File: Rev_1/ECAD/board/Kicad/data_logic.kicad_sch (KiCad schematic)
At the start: 7 parts

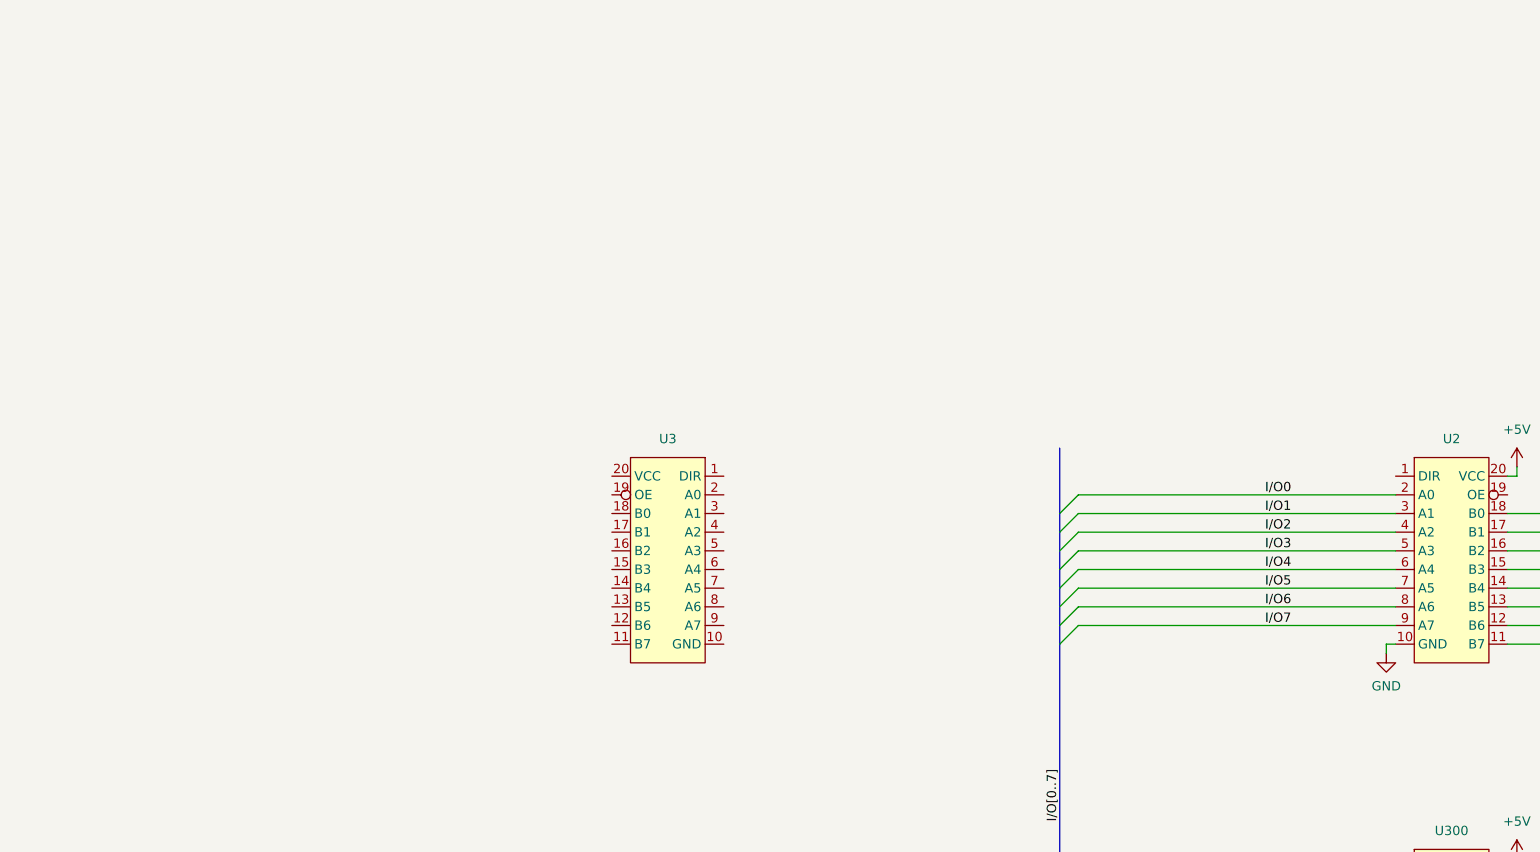
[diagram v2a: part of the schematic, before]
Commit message: Added Rotary encoder and buttons to the Input Buffer
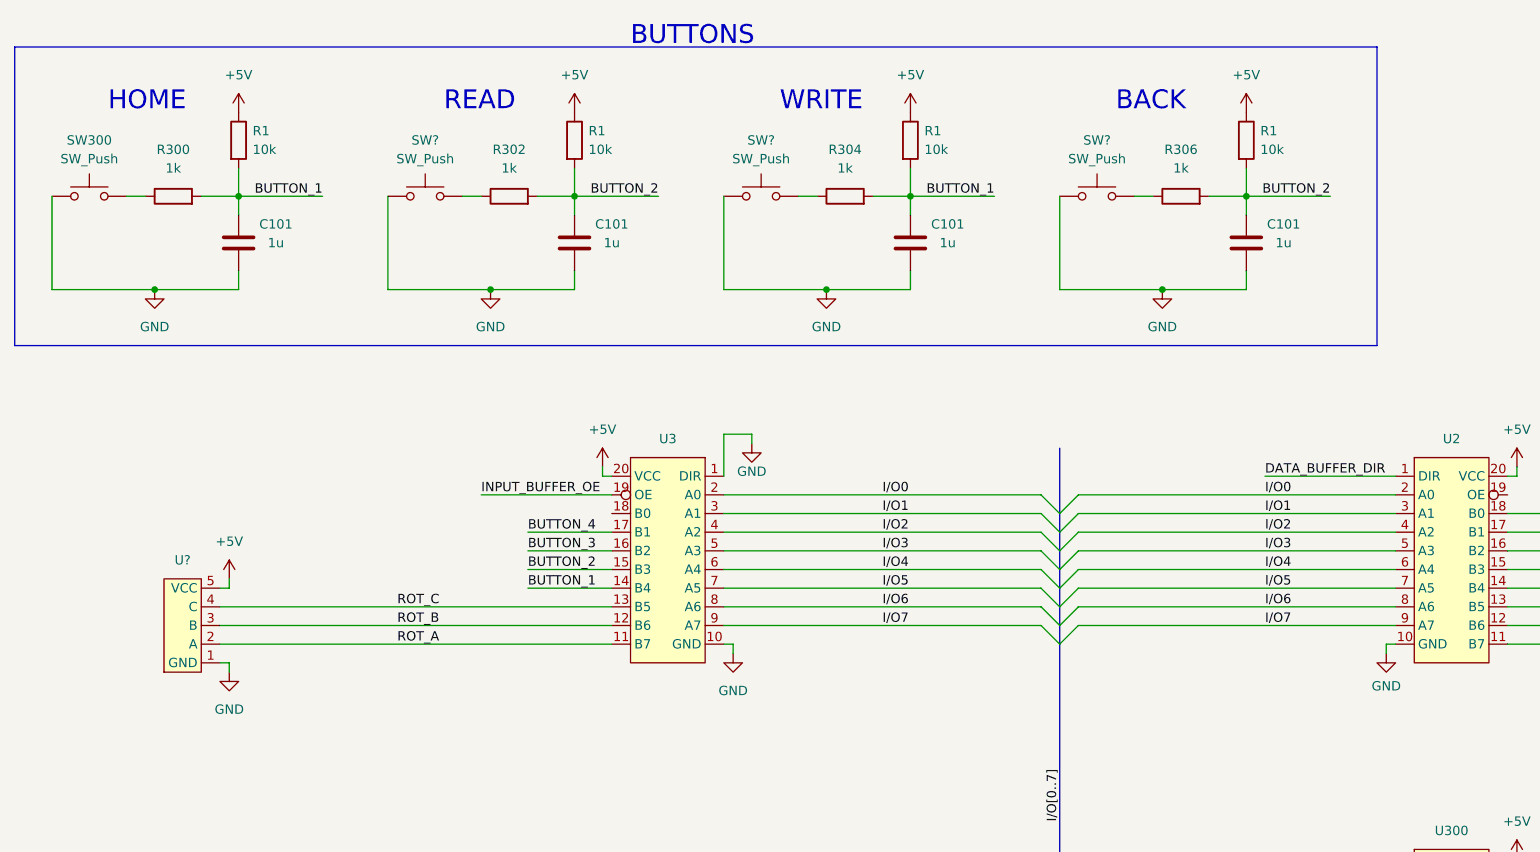
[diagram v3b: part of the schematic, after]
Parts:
- added C101 (x4): 1u, Capacitor_SMD:C_0805_2012Metric_Pad1.18x1.45mm_HandSolder, symbol Device:C
- added R1 (x4): 10k, Resistor_SMD:R_0805_2012Metric_Pad1.20x1.40mm_HandSolder, symbol Device:R
- added R300, R302, R304, R306: 1k, Resistor_SMD:R_0805_2012Metric_Pad1.20x1.40mm_HandSolder, symbol Device:R
- added SW300, SW? (x3): SW_Push, symbol Switch:SW_Push
- added U?: ~, symbol EEPROM_PROGRAMER:Rotary_Encoder
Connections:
- net +5V: now also U3.20 (VCC), R1.1, R1.1, R1.1, R1.1, U?.5 (VCC)
- net GND: now also U3.1 (DIR), U3.10 (GND), C101.1, C101.1, C101.1, C101.1, SW300.1, SW?.1, SW?.1, SW?.1, U?.1 (GND)
- net I/O0: now also U3.2 (A0)
- net I/O1: now also U3.3 (A1)
- net I/O2: now also U3.4 (A2)
- net I/O3: now also U3.5 (A3)
- net I/O4: now also U3.6 (A4)
- net I/O5: now also U3.7 (A5)
- net I/O6: now also U3.8 (A6)
- net I/O7: now also U3.9 (A7)
- net ROT_A: now reaches U3.11 (B7)
- net ROT_A: now also U?.2 (A)
- net ROT_B: now reaches U3.12 (B6)
- net ROT_B: now also U?.3 (B)
- net ROT_C: now reaches U3.13 (B5)
- net ROT_C: now also U?.4 (C)
- net BUTTON_1: now reaches U3.14 (B4)
- net BUTTON_1: now also C101.2, C101.2, R1.2, R1.2, R300.2, R304.2
- net BUTTON_2: now reaches U3.15 (B3)
- net BUTTON_2: now also C101.2, C101.2, R1.2, R1.2, R302.2, R306.2
- net BUTTON_3: now reaches U3.16 (B2)
- net BUTTON_4: now reaches U3.17 (B1)
- net INPUT_BUFFER_OE: now reaches U3.19 (OE)
- net DATA_BUFFER_DIR: now reaches U2.1 (DIR)
- new net: R304.1, SW?.2
- new net: R302.1, SW?.2
- new net: R300.1, SW300.2
- new net: R306.1, SW?.2
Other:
- note added: "BACK"
- note added: "BUTTONS"
- note added: "HOME"
- note added: "READ"
- note added: "WRITE"

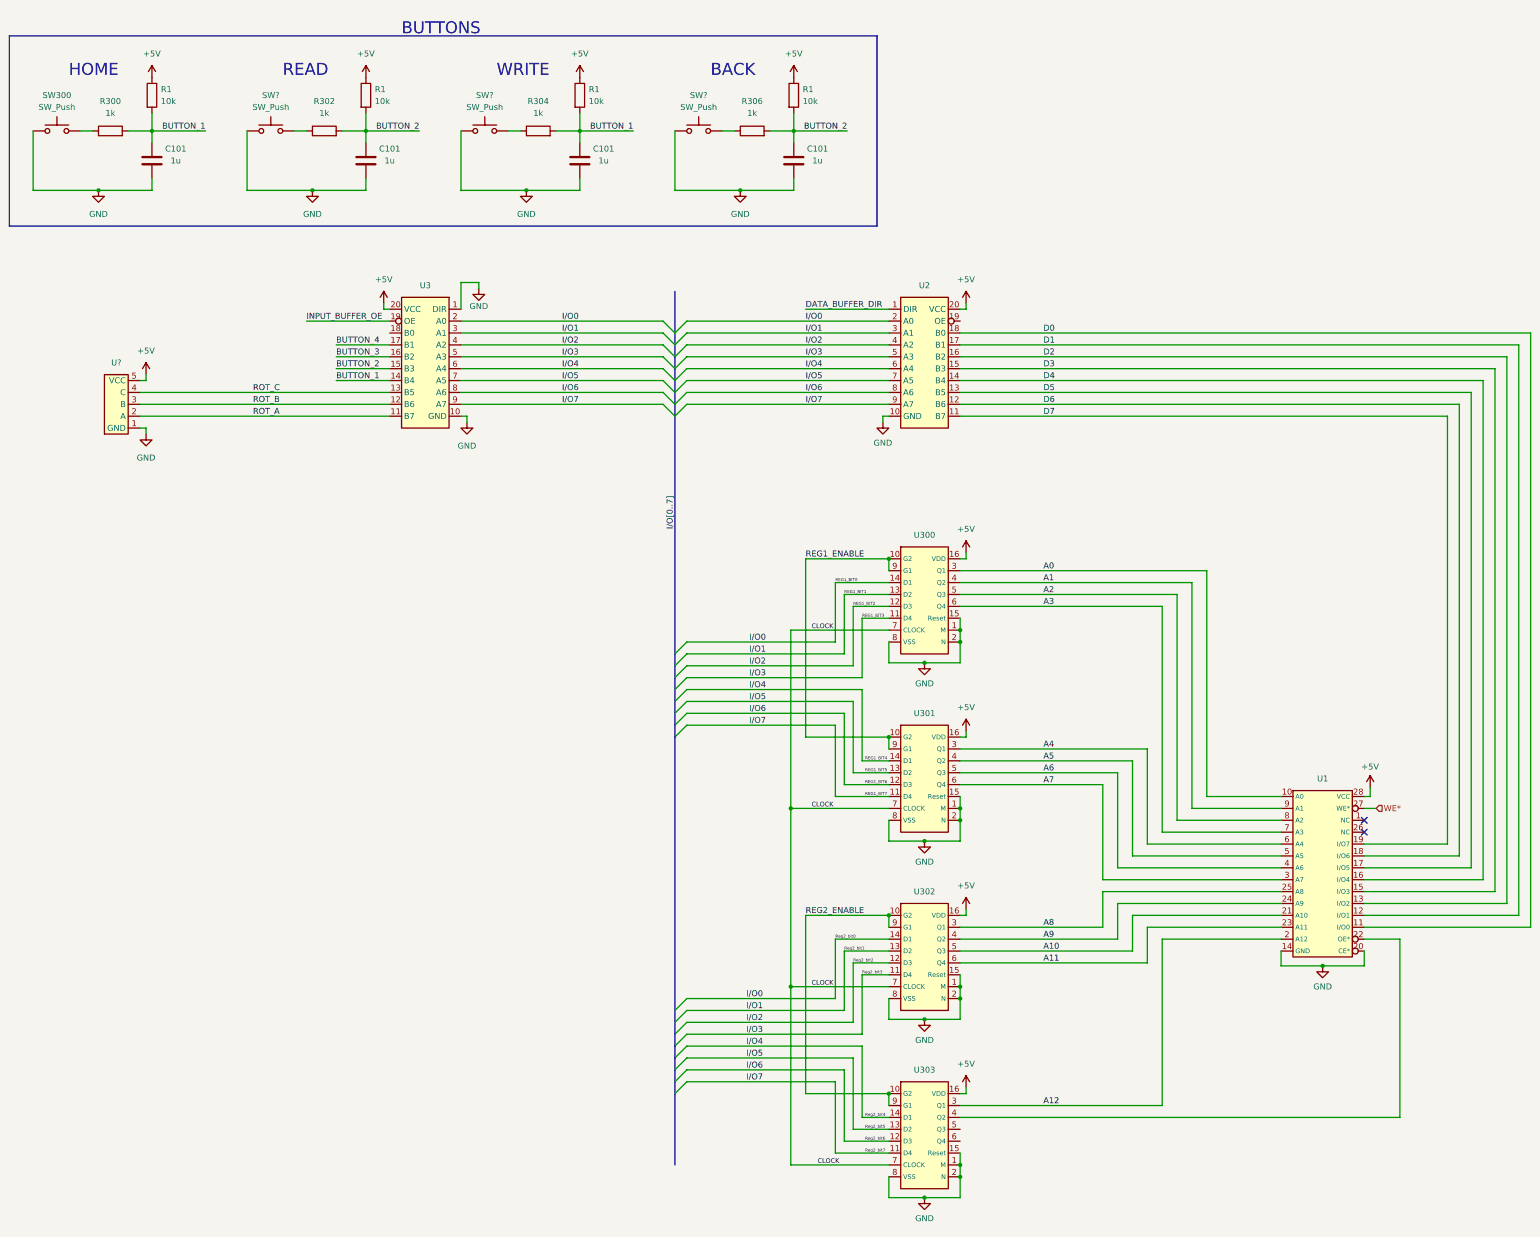
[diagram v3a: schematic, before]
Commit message: Updated gitignore
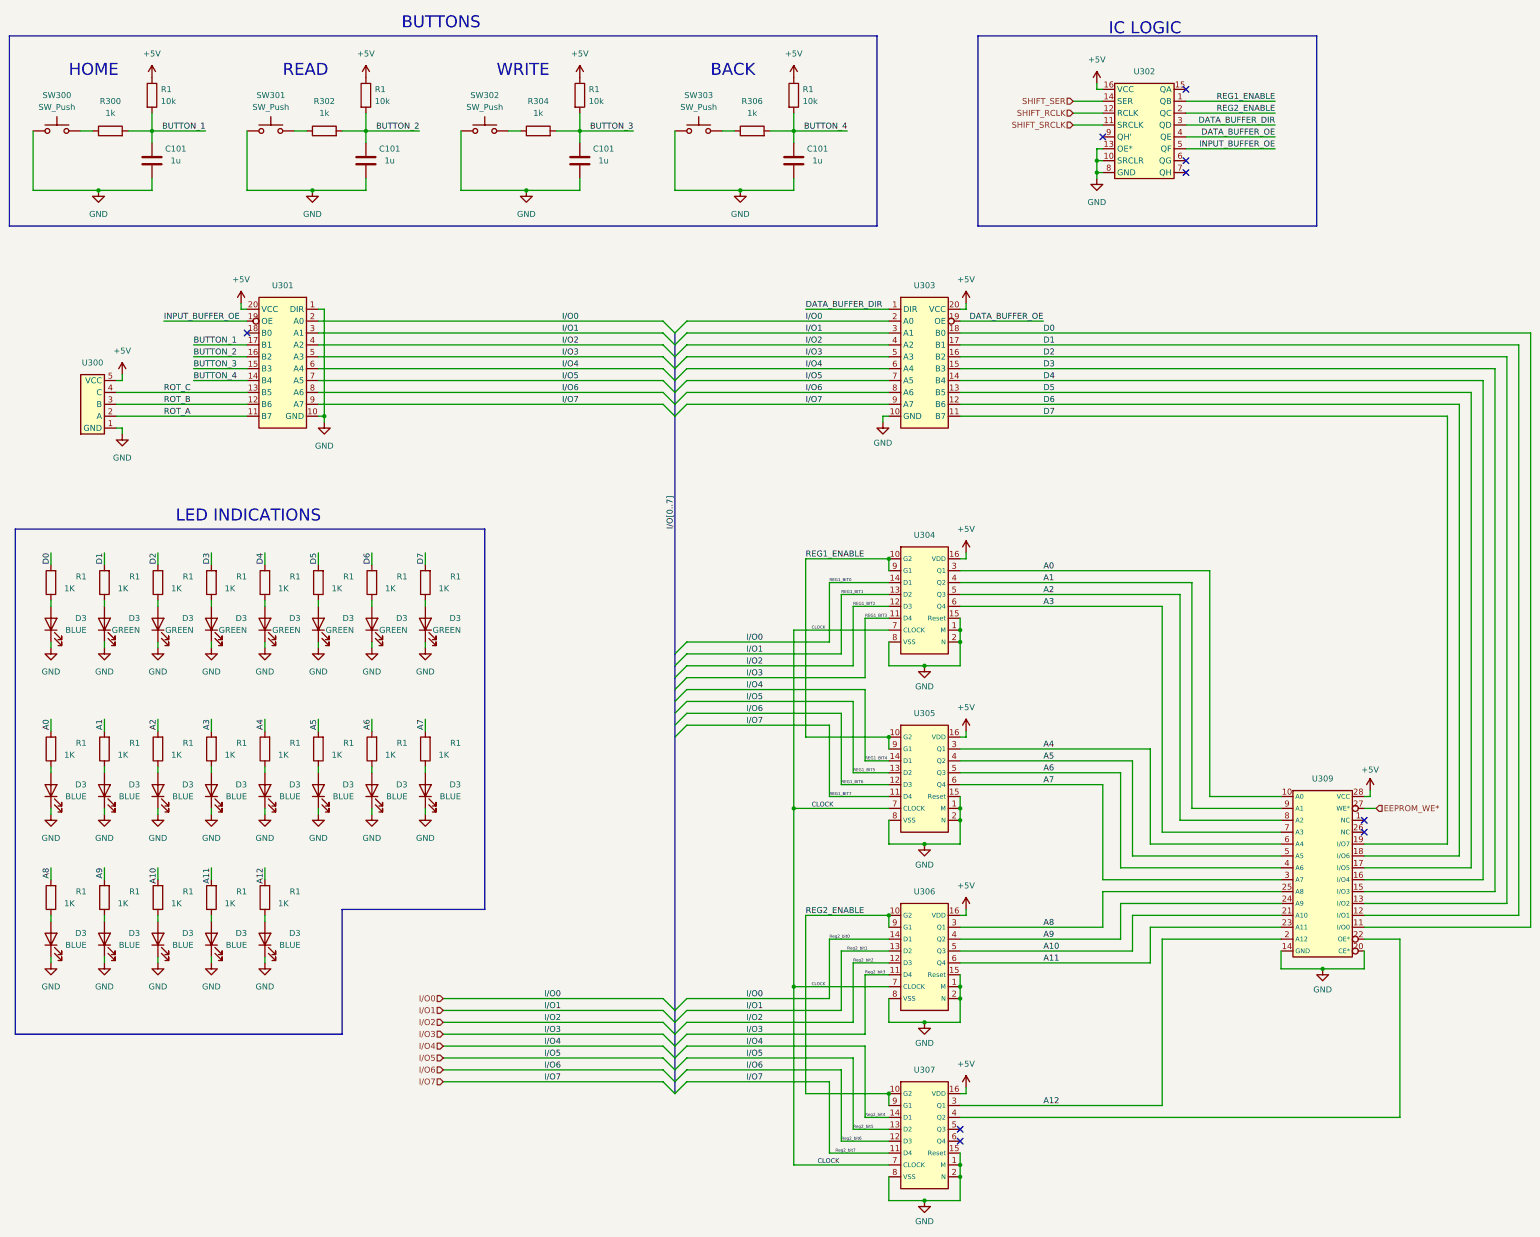
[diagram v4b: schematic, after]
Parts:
- added D3 (x14): BLUE, LED_SMD:LED_0805_2012Metric_Pad1.15x1.40mm_HandSolder, symbol Device:LED
- added D3 (x7): GREEN, LED_SMD:LED_0805_2012Metric_Pad1.15x1.40mm_HandSolder, symbol Device:LED
- added R1 (x21): 1K, Resistor_SMD:R_0805_2012Metric_Pad1.20x1.40mm_HandSolder, symbol Device:R
- added U302: ~, symbol EEPROM_PROGRAMER:74HC595
- gave numbers to parts that had none: 4
- renumbered U3 to U301, U2 to U303, U300 to U304, U301 to U305, U302 to U306, U303 to U307, U1 to U309
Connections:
- net +5V: now also U302.16 (VCC)
- net A0: now also R1.2
- net A1: now also R1.2
- net A10: now also R1.2
- net A11: now also R1.2
- net A12: now also R1.2
- net A2: now also R1.2
- net A3: now also R1.2
- net A4: now also R1.2
- net A5: now also R1.2
- net A6: now also R1.2
- net A7: now also R1.2
- net A8: now also R1.2
- net A9: now also R1.2
- net BUTTON_1: now also U301.17 (B1); no longer C101.2, R1.2, R304.2, U301.14 (B4)
- net BUTTON_2: now also U301.16 (B2); no longer C101.2, R1.2, R306.2, U301.15 (B3)
- net BUTTON_3: now also C101.2, R1.2, R304.2, U301.15 (B3); no longer U301.16 (B2)
- net BUTTON_4: now also C101.2, R1.2, R306.2, U301.14 (B4); no longer U301.17 (B1)
- net D0: now also R1.2
- net D1: now also R1.2
- net D2: now also R1.2
- net D3: now also R1.2
- net D4: now also R1.2
- net D5: now also R1.2
- net D6: now also R1.2
- net D7: now also R1.2
- net DATA_BUFFER_DIR: now also U302.3 (QD)
- net GND: now also D3.1 (K), D3.1 (K), D3.1 (K), D3.1 (K), D3.1 (K), D3.1 (K), D3.1 (K), D3.1 (K), D3.1 (K), D3.1 (K), D3.1 (K), D3.1 (K), D3.1 (K), D3.1 (K), D3.1 (K), D3.1 (K), D3.1 (K), D3.1 (K), D3.1 (K), D3.1 (K), D3.1 (K), U302.10 (SRCLR), U302.13 (OE*), U302.8 (GND)
- net INPUT_BUFFER_OE: now also U302.5 (QF)
- net REG1_ENABLE: now also U302.1 (QB)
- net REG2_ENABLE: now also U302.2 (QC)
- net DATA_BUFFER_OE: now reaches U303.19 (OE)
- net DATA_BUFFER_OE: now also U302.4 (QE)
- net I/O0 renamed I/O0
- net I/O1 renamed I/O1
- net I/O2 renamed I/O2
- net I/O3 renamed I/O3
- net I/O4 renamed I/O4
- net I/O5 renamed I/O5
- net I/O6 renamed I/O6
- net I/O7 renamed I/O7
- net WE* renamed EEPROM_WE*
- new net: D3.2 (A), R1.1 (x21)
- new net SHIFT_RCLK: U302.12 (RCLK)
- new net SHIFT_SER: U302.14 (SER)
- new net SHIFT_SRCLK: U302.11 (SRCLK)
- no-connect marks 2 -> 9
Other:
- note added: "IC LOGIC"
- note added: "LED INDICATIONS"
- moved on the sheet: U300, U301
